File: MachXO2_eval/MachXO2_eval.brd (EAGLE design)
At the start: 72 x 95 mm, 29 parts, among them U1 LCMXO2-256HC-4TG100C, U2 AE-FT2232, U3 XC6202P332TH

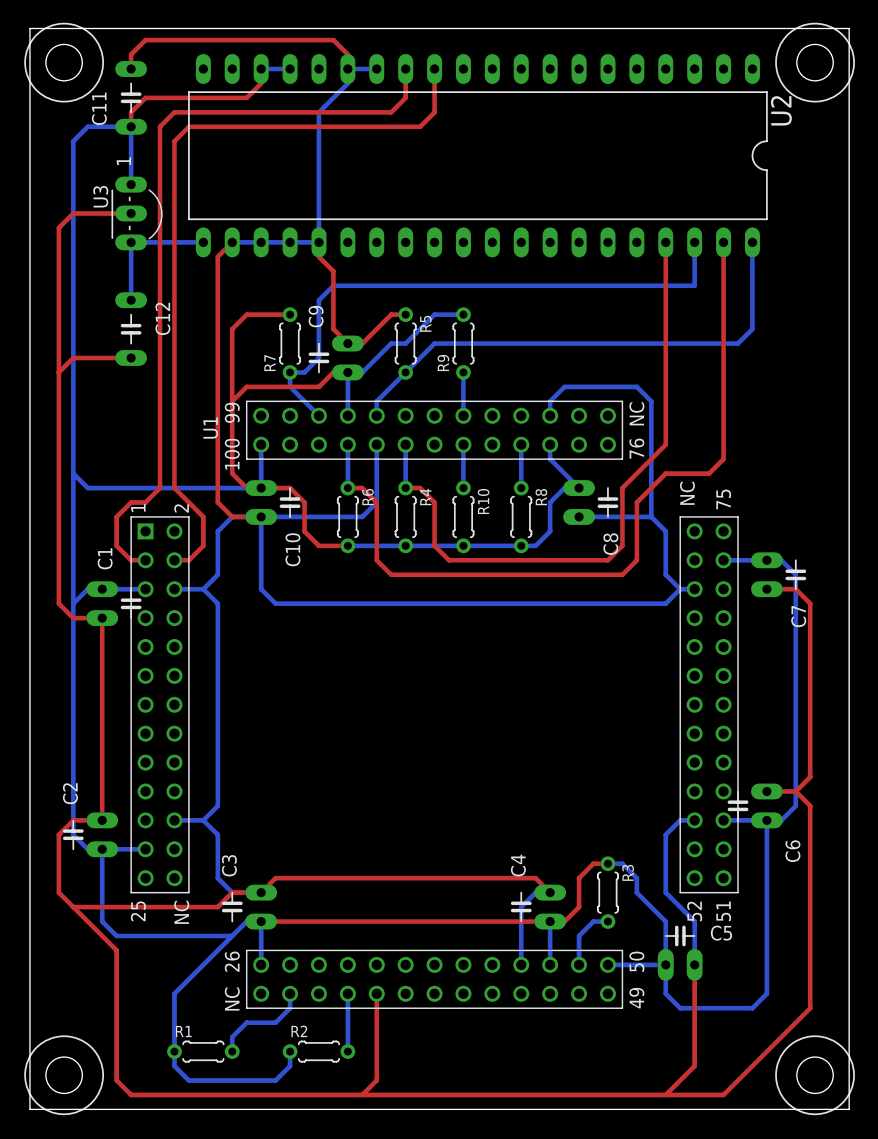
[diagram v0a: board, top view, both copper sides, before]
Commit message: ピンを増設
・動作確認用のピンを基板外に出すための配線を追加
・外部電源コネクターとケミコンを追加
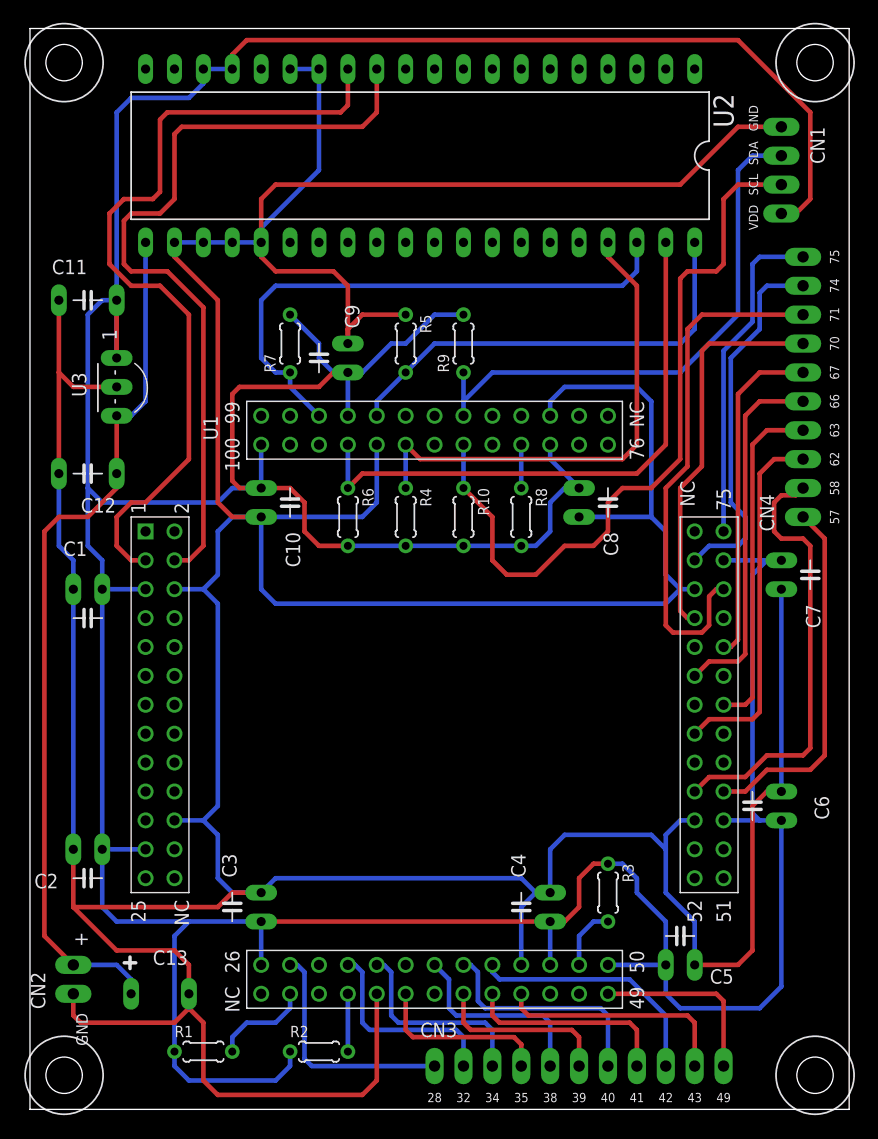
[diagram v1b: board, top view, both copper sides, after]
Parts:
- added C13: 10uF, Parts:ELECAP_200MIL
- added CN1: I2C_IF, PartsForProto:I2C_IF_4PIN
- added CN2: POWER_IF, PartsForProto:HEADER_2PIN_POWER_IF
- added CN3: LCMXO2-CN2, PartsForProto:LCMXO2-CN-11PIN
- added CN4: LCMXO2-CN1, PartsForProto:LCMXO2-CN-1
- moved C11 18.2 mm to (5.08, 71.1), turned to 180 degrees
- moved U3 15.3 mm to (7.62, 66.0)
- moved C12 13.3 mm to (5.08, 55.9), turned to 180 degrees
- moved U2 5.08 mm to (34.3, 83.8)
- moved C2 1.80 mm to (5.08, 22.9), turned to 180 degrees
- moved C1 1.80 mm to (5.08, 45.7), turned to 180 degrees
- moved C6 1.27 mm to (66.0, 26.7)
- moved C7 1.27 mm to (66.0, 47.0)
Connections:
- new net N$11: CN4.1, U1.57
- new net N$12: CN4.2, U1.58
- new net N$13: CN4.3, U1.62
- new net N$17: CN3.10, U1.43
- new net N$18: CN3.9, U1.42
- new net N$19: CN3.8, U1.41
- new net N$20: CN3.7, U1.40
- new net N$21: CN3.6, U1.39
- new net N$22: CN3.5, U1.38
- new net N$23: CN3.11, U1.49
- new net N$24: CN3.4, U1.35
- new net N$25: CN3.3, U1.34
- new net N$26: CN3.2, U1.32
- new net N$27: CN3.1, U1.28
- new net N$28: CN4.7, U1.70
- new net N$29: CN4.8, U1.71
- new net N$4: CN4.9, U1.74
- new net N$5: CN4.10, U1.75
- new net N$6: CN4.6, U1.67
- new net N$7: CN4.5, U1.66
- new net N$9: CN4.4, U1.63
- net +3V3: now also CN1.4
- net +5V: now also C13.+, CN2.2
- net 0V: now also C13.-, CN1.1, CN2.1
- net I2C_SCL: now also CN1.3
- net N$2: now also CN1.2
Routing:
- net +5V: track 11.4 -> 77.3 mm
- net I2C_SCL: track 3.81 -> 65.5 mm
- net +3V3: track 380.1 -> 435.0 mm
- net N$29: track 0.00 -> 45.9 mm
- net N$2: track 3.81 -> 48.1 mm
- net N$12: track 0.00 -> 38.8 mm
- net N$28: track 0.00 -> 34.3 mm
- net N$4: track 0.00 -> 32.5 mm
- net N$11: track 0.00 -> 31.9 mm
- net N$13: track 0.00 -> 31.8 mm
- net N$7: track 0.00 -> 31.8 mm
- net N$9: track 0.00 -> 30.0 mm
- net N$6: track 0.00 -> 29.6 mm
- net N$5: track 0.00 -> 29.3 mm
- net N$18: track 0.00 -> 21.9 mm
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
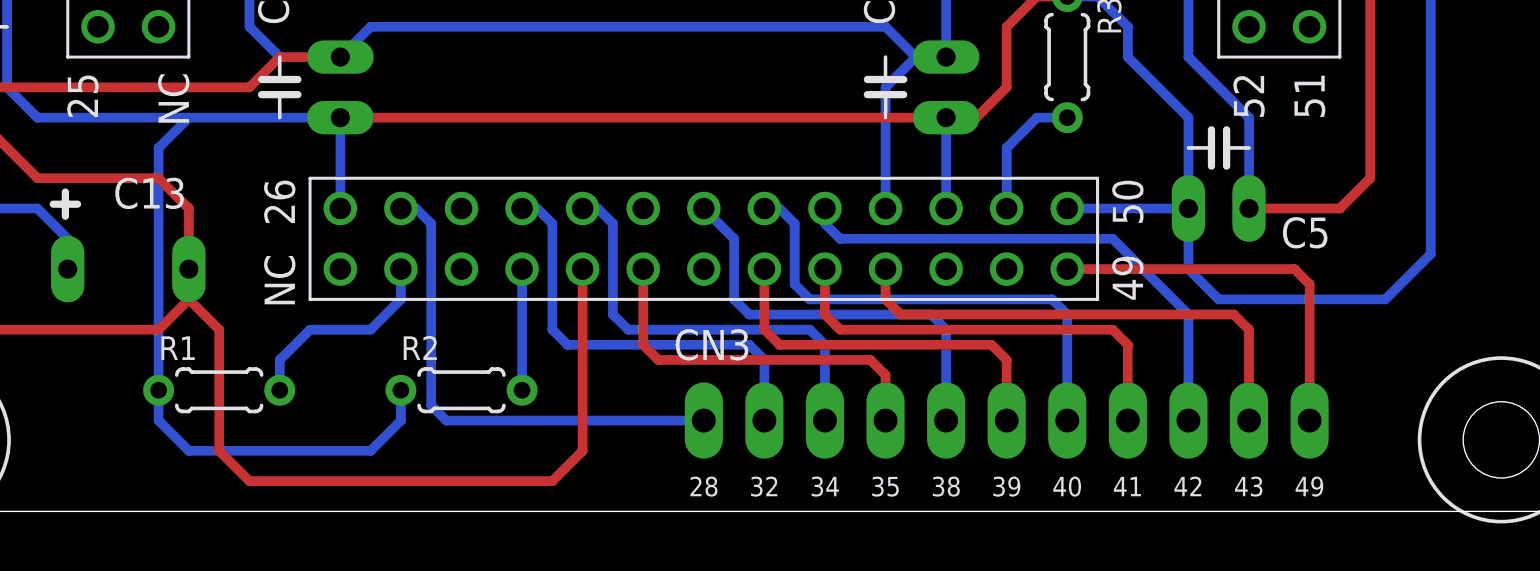
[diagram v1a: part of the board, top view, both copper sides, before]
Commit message: MachXO2評価基板修正
外出しピンを追加
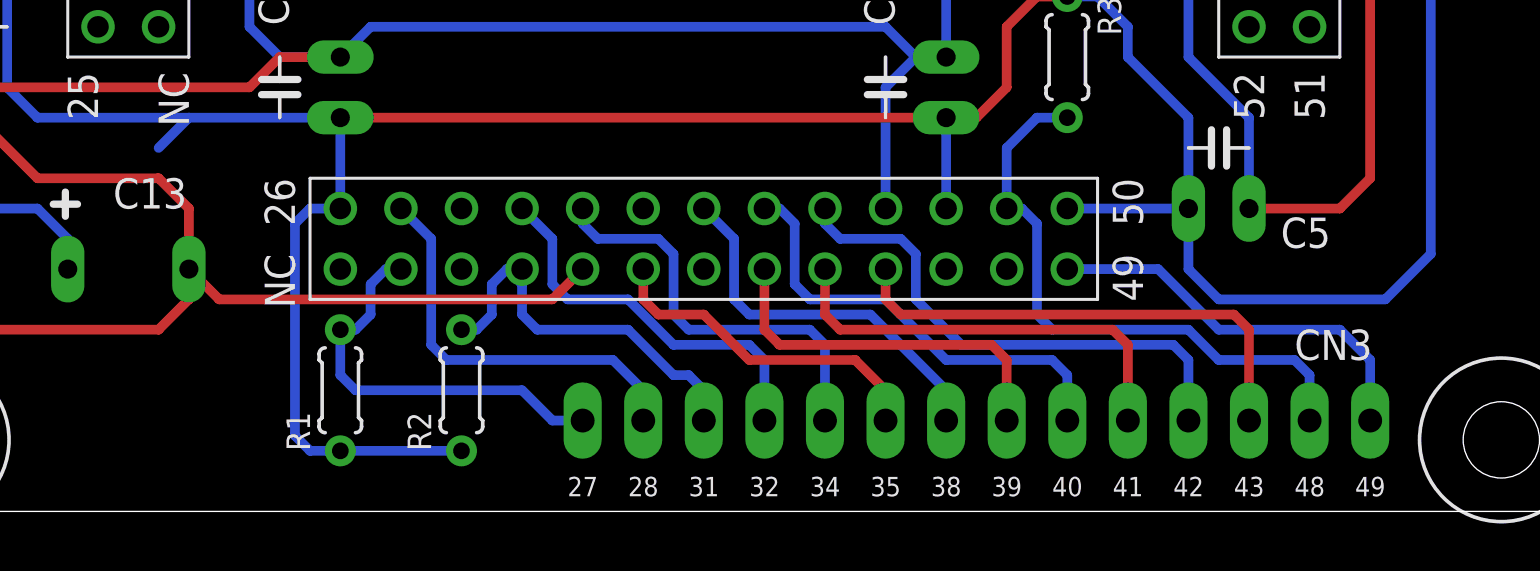
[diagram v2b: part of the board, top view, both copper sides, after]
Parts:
- CN3: device PartsForProto:LCMXO2-CN-11PIN -> PartsForProto:LCMXO2-CN-2
- moved CN3 5.08 mm to (30.5, 3.81)
- moved R1 5.08 mm to (20.3, 5.08), turned to 90 degrees
- turned R2 to 90 degrees
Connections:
- removed net N$23: CN3.11, U1.49
- new net N$14: CN3.14, U1.49
- net N$10: now also CN3.13
- net N$17: now also CN3.12; no longer CN3.10
- net N$18: now also CN3.11; no longer CN3.9
- net N$19: now also CN3.10; no longer CN3.8
- net N$20: now also CN3.9; no longer CN3.7
- net N$21: now also CN3.8; no longer CN3.6
- net N$22: now also CN3.7; no longer CN3.5
- net N$24: now also CN3.6; no longer CN3.4
- net N$25: now also CN3.5; no longer CN3.3
- net N$26: now also CN3.4; no longer CN3.2
- net N$27: now also CN3.2; no longer CN3.1
- net N$3: now also CN3.1
- net N$8: now also CN3.3
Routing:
- net N$10: track 5.61 -> 25.3 mm
- net N$14: track 0.00 -> 16.8 mm
- net N$23: track 16.1 -> 0.00 mm
- net 0V: track 512.3 -> 499.1 mm
- net N$8: track 5.08 -> 16.7 mm
- net N$3: track 8.67 -> 17.2 mm
- net +3V3: track 435.0 -> 429.3 mm
- net N$27: track 20.8 -> 17.2 mm
- net N$24: track 15.8 -> 14.3 mm
- net N$26: track 17.9 -> 16.4 mm
- net N$22: track 17.6 -> 16.1 mm
- net N$20: track 20.5 -> 19.0 mm

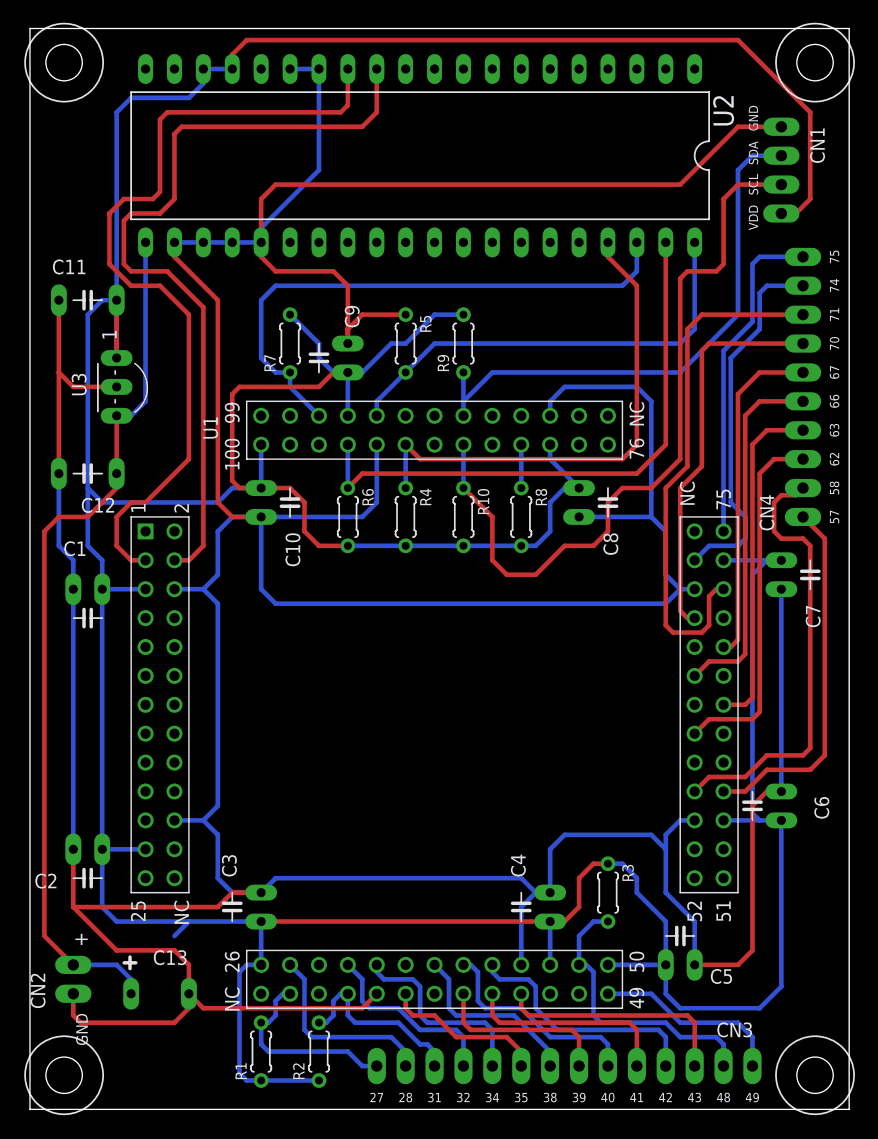
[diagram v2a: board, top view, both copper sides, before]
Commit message: MachXO2評価基板修正
外出し用のピンを追加
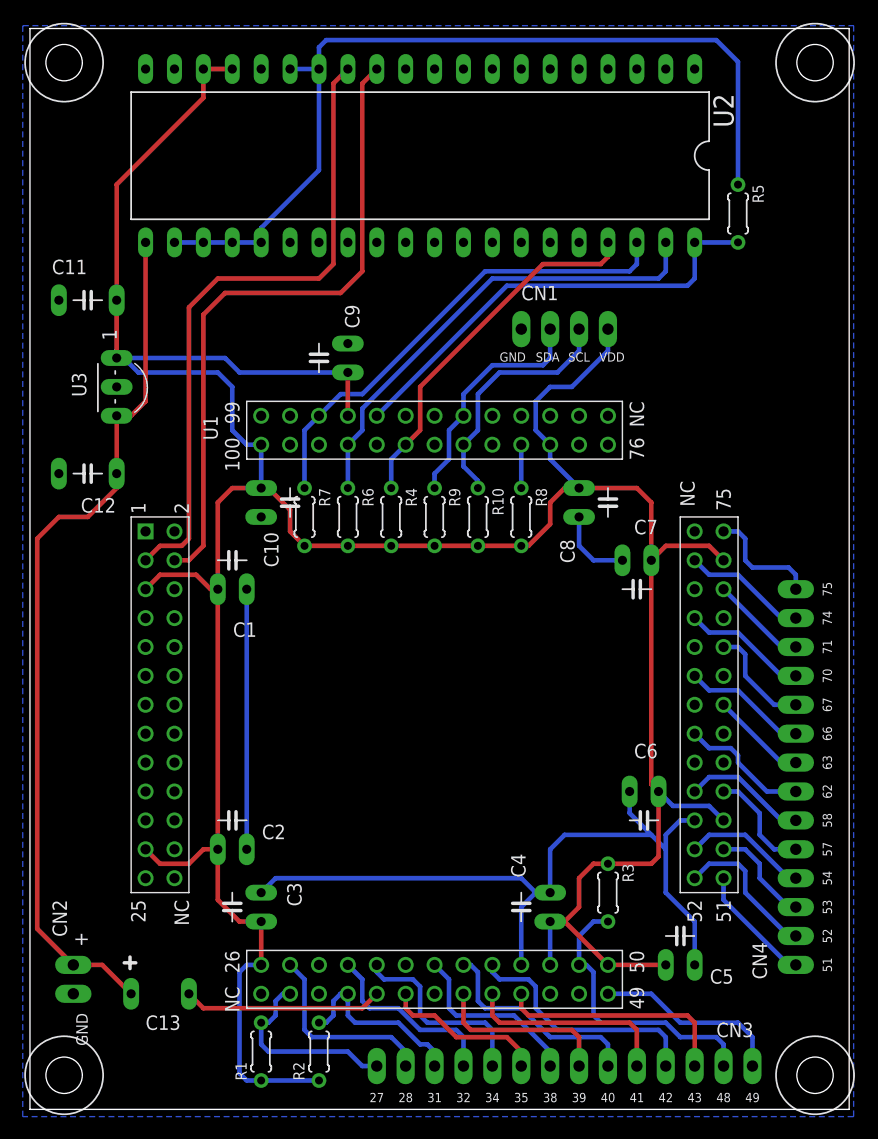
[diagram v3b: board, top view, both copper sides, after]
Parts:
- moved CN4 39.4 mm to (67.3, 12.7)
- moved R5 31.4 mm to (62.2, 78.7)
- moved CN1 29.0 mm to (43.2, 68.6), turned to 0 degrees
- moved R9 15.5 mm to (35.6, 52.1), turned to 270 degrees
- moved R7 15.3 mm to (24.1, 52.1), turned to 270 degrees
- moved C7 12.8 mm to (53.3, 48.3), turned to 180 degrees
- moved C1 12.7 mm to (17.8, 45.7), turned to 0 degrees
- moved C2 12.7 mm to (17.8, 22.9), turned to 0 degrees
- moved C6 12.1 mm to (54.0, 27.9), turned to 180 degrees
- moved R4 1.27 mm to (31.8, 52.1)
- moved R10 1.27 mm to (39.4, 52.1)
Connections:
- new net N$15: CN4.2, U1.52
- new net N$16: CN4.1, U1.51
- new net N$23: CN4.13, U1.74
- new net N$30: CN4.14, U1.75
- net N$11: now also CN4.5; no longer CN4.1
- net N$12: now also CN4.6; no longer CN4.2
- net N$13: now also CN4.7; no longer CN4.3
- net N$28: now also CN4.11; no longer CN4.7
- net N$29: now also CN4.12; no longer CN4.8
- net N$4: now also CN4.4, U1.54; no longer CN4.9, U1.74
- net N$5: now also CN4.3, U1.53; no longer CN4.10, U1.75
- net N$6: now also CN4.10; no longer CN4.6
- net N$7: now also CN4.9; no longer CN4.5
- net N$9: now also CN4.8; no longer CN4.4
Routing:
- net 0V: track 499.1 -> 193.9 mm
- net +3V3: track 429.3 -> 297.5 mm
- net I2C_SCL: track 65.5 -> 21.7 mm
- net N$29: track 45.9 -> 8.45 mm
- net N$12: track 38.8 -> 11.0 mm
- net N$2: track 48.1 -> 20.8 mm
- net N$28: track 34.3 -> 11.0 mm
- net N$11: track 31.9 -> 9.57 mm
- net N$9: track 30.0 -> 8.45 mm
- net N$4: track 32.5 -> 11.0 mm
- net N$7: track 31.8 -> 11.0 mm
- net N$13: track 31.8 -> 11.4 mm
- net N$5: track 29.3 -> 9.20 mm
- net N$6: track 29.6 -> 9.57 mm
- net FT2232_BD0: track 71.8 -> 56.9 mm
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- added copper zone on layer 16, net 0V

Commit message: MachXO2評価基板修正
外出し用のピンをさらに追加
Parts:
- added CN5: I2C_IF, PartsForProto:I2C_IF_4PIN
- added CN6: POWER_IF, PartsForProto:HEADER_2PIN_POWER_IF
- added FB1: BLM21PG300SN1D, Parts:SMD_2012
- CN1: value I2C_IF -> LCMXO2-CN3; device PartsForProto:I2C_IF_4PIN -> PartsForProto:LCMXO2-CN-3
- CN2: value POWER_IF -> LCMXO2-CN2; device PartsForProto:HEADER_2PIN_POWER_IF -> PartsForProto:LCMXO2-CN-2
- CN3: value LCMXO2-CN2 -> LCMXO2-CN1; device PartsForProto:LCMXO2-CN-2 -> PartsForProto:LCMXO2-CN-1
- CN4: value LCMXO2-CN1 -> LCMXO2-CN4; device PartsForProto:LCMXO2-CN-1 -> PartsForProto:LCMXO2-CN-4
- moved CN1 44.3 mm to (3.81, 48.3), turned to 270 degrees
- moved CN4 41.9 mm to (67.3, 54.6)
- moved CN3 37.9 mm to (67.3, 12.7), turned to 90 degrees
- moved CN2 27.4 mm to (30.5, 3.81), turned to 0 degrees
- moved C12 2.84 mm to (3.81, 58.4), turned to 270 degrees
- moved C6 2.54 mm to (54.0, 25.4)
- moved C7 2.54 mm to (53.3, 50.8)
- moved C1 1.27 mm to (16.5, 45.7), turned to 270 degrees
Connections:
- new net N$31: CN4.1, U1.76
- new net N$32: CN4.2, U1.77
- new net N$33: C12.1, FB1.1, U3.3
- new net N$35: CN4.8, U1.99
- new net N$36: CN4.7, U1.98
- new net N$37: CN4.6, U1.88
- new net N$38: CN4.5, U1.87
- new net N$39: CN4.3, U1.81
- new net N$43: CN1.12, U1.25
- new net N$44: CN1.11, U1.24
- new net N$46: CN1.10, U1.21
- new net N$47: CN1.9, U1.20
- new net N$48: CN1.8, U1.17
- new net N$49: CN1.7, U1.16
- new net N$50: CN1.6, U1.13
- new net N$51: CN1.5, U1.12
- new net N$52: CN1.4, U1.8
- new net N$53: CN1.3, U1.7
- new net N$54: CN1.2, U1.2
- new net N$55: CN1.1, U1.1
- net +3V3: now also CN5.4; no longer CN1.4
- net +5V: now also CN6.2, FB1.2; no longer C12.1, CN2.2, U3.3
- net 0V: now also CN5.1, CN6.1; no longer CN1.1, CN2.1
- net I2C_SCL: now also CN5.3; no longer CN1.3
- net N$1: now also CN4.4
- net N$10: now also CN2.13; no longer CN3.13
- net N$11: now also CN3.5; no longer CN4.5
- net N$12: now also CN3.6; no longer CN4.6
- net N$13: now also CN3.7; no longer CN4.7
- net N$14: now also CN2.14; no longer CN3.14
- net N$15: now also CN3.2; no longer CN4.2
- net N$16: now also CN3.1; no longer CN4.1
- net N$17: now also CN2.12; no longer CN3.12
- net N$18: now also CN2.11; no longer CN3.11
- net N$19: now also CN2.10; no longer CN3.10
- net N$2: now also CN5.2; no longer CN1.2
- net N$20: now also CN2.9; no longer CN3.9
- net N$21: now also CN2.8; no longer CN3.8
- net N$22: now also CN2.7; no longer CN3.7
- net N$23: now also CN3.13; no longer CN4.13
- net N$24: now also CN2.6; no longer CN3.6
- net N$25: now also CN2.5; no longer CN3.5
- net N$26: now also CN2.4; no longer CN3.4
- net N$27: now also CN2.2; no longer CN3.2
- net N$28: now also CN3.11; no longer CN4.11
- net N$29: now also CN3.12; no longer CN4.12
- net N$3: now also CN2.1; no longer CN3.1
- net N$30: now also CN3.14; no longer CN4.14
- net N$4: now also CN3.4; no longer CN4.4
- net N$5: now also CN3.3; no longer CN4.3
- net N$6: now also CN3.10; no longer CN4.10
- net N$7: now also CN3.9; no longer CN4.9
- net N$8: now also CN2.3; no longer CN3.3
- net N$9: now also CN3.8; no longer CN4.8
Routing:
- net 0V: track 193.9 -> 106.0 mm
- net N$36: track 0.00 -> 54.3 mm
- net N$35: track 0.00 -> 54.0 mm
- net N$37: track 0.00 -> 39.1 mm
- net N$38: track 0.00 -> 33.5 mm
- net N$1: track 3.81 -> 34.6 mm
- net N$39: track 0.00 -> 25.7 mm, vias 0 -> 1
- net N$32: track 0.00 -> 20.6 mm, vias 0 -> 1
- net N$31: track 0.00 -> 18.1 mm, vias 0 -> 1
- net N$54: track 0.00 -> 13.5 mm
- net N$51: track 0.00 -> 9.94 mm
- net N$52: track 0.00 -> 9.94 mm
- net N$47: track 0.00 -> 9.94 mm
- net N$44: track 0.00 -> 9.94 mm
- net N$49: track 0.00 -> 9.94 mm
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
